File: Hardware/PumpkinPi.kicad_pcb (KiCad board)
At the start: 2 copper layers, 12.1 x 13.3 mm, 30 parts, among them J1 Conn_01x02_Male, J2 Conn_01x04, J3 Micro_SD_Card, U1 F1C100s, U2 EA3036, Y1 Crystal_GND24

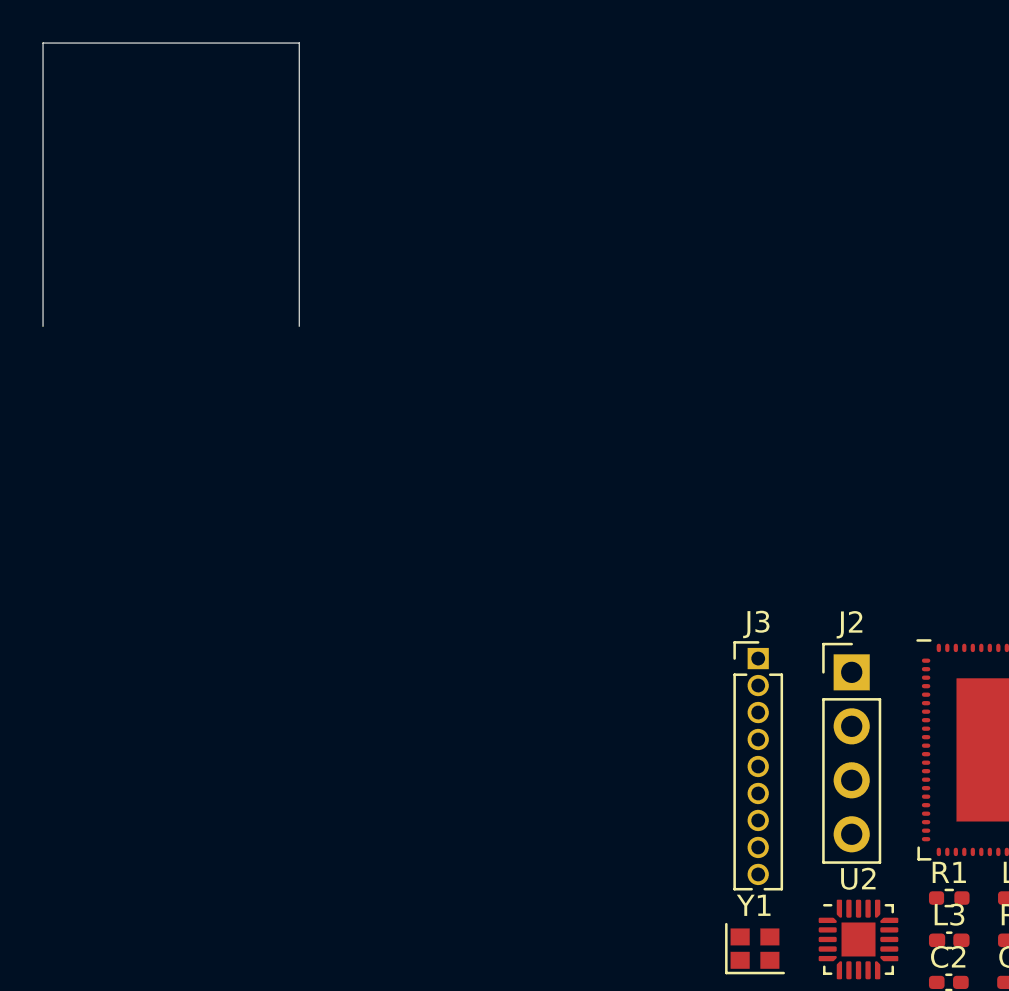
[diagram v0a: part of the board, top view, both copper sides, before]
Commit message: USB connector
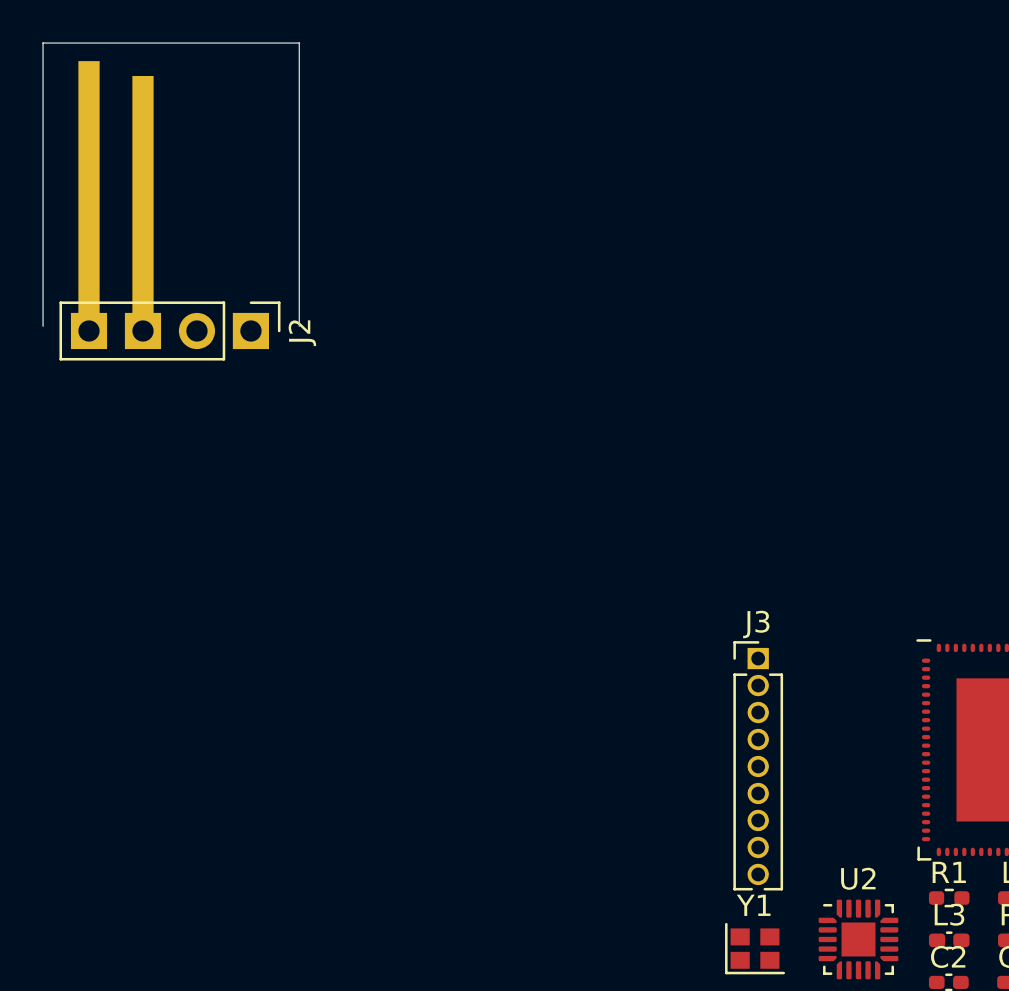
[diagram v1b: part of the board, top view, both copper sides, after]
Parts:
- moved J2 32.5 mm to (109.8, 83.6), turned to 270 degrees

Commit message: progress on wiring
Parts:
- U1: moved to B.Cu
- moved U1 42.0 mm to (106.0, 91.4)
- moved R1 35.4 mm to (176.9, 119.1)
- moved R2 33.8 mm to (185.4, 118.1)
- moved C4 31.3 mm to (181.6, 124.5)
- moved J3 29.8 mm to (104.1, 102.9)
- moved R3 28.8 mm to (181.6, 113.0)
- moved C1 21.7 mm to (174.0, 112.8)
- moved C2 20.8 mm to (155.3, 130.7)
- moved C3 20.8 mm to (158.5, 130.7)
- moved L1 20.4 mm to (168.9, 116.8)
- moved L3 17.6 mm to (146.1, 129.5)
- moved L2 15.5 mm to (145.5, 125.7)
- moved R5 14.3 mm to (157.5, 120.7)
- moved U2 11.0 mm to (133.3, 121.9)
- moved J1 6.75 mm to (149.9, 94.0)
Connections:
- C1 pad 2: GND -> /FB1
- C2 pad 2: GND -> /FB1
- C3 pad 2: GND -> /FB1
- R1 pad 2: GND -> /FB1
- R2 pad 1: GND -> /FB1
- R3 pad 2: GND -> /FB1
- R4 pad 1: GND -> /FB1
- R5 pad 2: GND -> /FB1
- R6 pad 1: GND -> /FB1
- U2 pad 14: GND -> /FB1

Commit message: wiring in progress
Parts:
- moved R8 53.9 mm to (202.4, 101.8)
- moved C12 49.8 mm to (202.2, 112.0)
- moved C7 44.6 mm to (130.1, 134.9), turned to 90 degrees
- moved C6 39.0 mm to (181.1, 133.9)
- moved R6 39.0 mm to (174.6, 137.8), turned to 270 degrees
- moved Y1 33.6 mm to (108.5, 90.1), turned to 90 degrees
- moved C11 33.4 mm to (190.3, 89.9)
- moved C5 32.8 mm to (179.3, 125.0)
- moved R4 32.8 mm to (174.5, 128.6), turned to 270 degrees
- moved C10 30.8 mm to (143.9, 134.7), turned to 90 degrees
- moved C9 30.5 mm to (138.3, 135.0), turned to 270 degrees
- moved C8 25.7 mm to (133.9, 134.9), turned to 90 degrees
- moved L3 22.1 mm to (167.8, 133.8), turned to 180 degrees
- moved R5 22.1 mm to (174.9, 134.3), turned to 270 degrees
- moved L2 21.8 mm to (167.2, 124.2)
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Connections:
- C2 pad 2: /FB1 -> /FB2
- C3 pad 2: /FB1 -> /FB3
- L2 pad 2: /LX1 -> /LX2
- L3 pad 2: /LX1 -> /LX3
- R3 pad 2: /FB1 -> /FB2
- R4 pad 1: /FB1 -> /FB2
- R5 pad 2: /FB1 -> /FB3
- R6 pad 1: /FB1 -> /FB3

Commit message: progress ...
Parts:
- removed C1, C2, C3: 220p, Capacitor_SMD:C_0402_1005Metric_Pad0.74x0.62mm_HandSolder
- removed C10: 1u, Capacitor_SMD:C_0402_1005Metric_Pad0.74x0.62mm_HandSolder
- removed C11, C12: 30p, Capacitor_SMD:C_0402_1005Metric_Pad0.74x0.62mm_HandSolder
- removed C4, C5, C6, C7, C8, C9: 10u, Capacitor_SMD:C_0402_1005Metric_Pad0.74x0.62mm_HandSolder
- removed J1: Conn_01x02_Male, Connector_PinHeader_1.27mm:PinHeader_1x02_P1.27mm_Vertical
- removed J2: Conn_01x04, Connector_PinHeader_2.54mm:PinHeader_1x04_P2.54mm_Vertical
- removed J3: Micro_SD_Card, Connector_PinHeader_1.27mm:PinHeader_1x09_P1.27mm_Vertical
- removed L1, L2, L3: 1.5u, Inductor_SMD:L_0402_1005Metric_Pad0.77x0.64mm_HandSolder
- removed R1, R2, R3, R4, R5, R6: 100k, Resistor_SMD:R_0402_1005Metric_Pad0.72x0.64mm_HandSolder
- removed R7: R, Resistor_SMD:R_0402_1005Metric_Pad0.72x0.64mm_HandSolder
- removed R8, R9: 2k2, Resistor_SMD:R_0402_1005Metric_Pad0.72x0.64mm_HandSolder
- removed U1: F1C100s, PumpkinPi:QFN-88_EP_10x10_Pitch0.4mm
- removed U2: EA3036, Package_DFN_QFN:QFN-20-1EP_3x3mm_P0.45mm_EP1.6x1.6mm
- removed Y1: Crystal_GND24, Crystal:Crystal_SMD_2016-4Pin_2.0x1.6mm
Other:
- board outline removed
- net class Default: trace_width 0.25 -> 0.2; via_dia 0.8 -> 0.4; via_drill 0.4 -> 0.3

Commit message: schemqtic finished, routing started
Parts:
- added C1: 1u, Capacitor_SMD:C_0402_1005Metric_Pad0.74x0.62mm_HandSolder, F.Cu at (159.8, 86.5)
- added C11: 30p, Capacitor_SMD:C_0402_1005Metric_Pad0.74x0.62mm_HandSolder, F.Cu at (162.2, 81.3)
- added C12: 30p, Capacitor_SMD:C_0402_1005Metric_Pad0.74x0.62mm_HandSolder, F.Cu at (162.2, 79.1)
- added C2: 1u, Capacitor_SMD:C_0402_1005Metric_Pad0.74x0.62mm_HandSolder, F.Cu at (159.8, 82.0)
- added C3: 1u, Capacitor_SMD:C_0402_1005Metric_Pad0.74x0.62mm_HandSolder, F.Cu at (159.8, 88.7)
- added J1: Conn_01x02_Male, Connector_PinHeader_1.00mm:PinHeader_1x02_P1.00mm_Vertical, F.Cu at (162.2, 90.9)
- added J2: Conn_01x04, Connector_PinHeader_2.54mm:PinHeader_1x04_P2.54mm_Vertical, F.Cu at (159.9, 92.0)
- added J3: 0475710001, MOLEX_0475710001, F.Cu at (153.0, 84.2)
- added R7: 51k, Resistor_SMD:R_0402_1005Metric_Pad0.72x0.64mm_HandSolder, F.Cu at (162.2, 88.1)
- added R8: 2k2, Resistor_SMD:R_0402_1005Metric_Pad0.72x0.64mm_HandSolder, F.Cu at (162.2, 83.6)
- added R9: 2k2, Resistor_SMD:R_0402_1005Metric_Pad0.72x0.64mm_HandSolder, F.Cu at (162.2, 85.8)
- added U1: F1C100s, PumpkinPi:QFN-88_EP_10x10_Pitch0.4mm, B.Cu at (155.7, 84.0)
- added U2: TPS717xx, Package_TO_SOT_SMD:SOT-353_SC-70-5, F.Cu at (157.7, 86.1)
- added U3: TPS717xx, Package_TO_SOT_SMD:SOT-353_SC-70-5, F.Cu at (157.7, 83.3)
- added U4: TPS717xx, Package_TO_SOT_SMD:SOT-353_SC-70-5, F.Cu at (157.7, 89.0)
- added Y1: Crystal_GND24, Crystal:Crystal_SMD_5032-4Pin_5.0x3.2mm, F.Cu at (158.9, 79.9)
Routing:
- net GND: track 0.00 -> 63.4 mm
- net /SVREF: track 0.00 -> 18.0 mm, vias 0 -> 2
- net /USB_VBUS: track 0.00 -> 15.9 mm
- net +1V1: track 0.00 -> 13.3 mm, vias 0 -> 2
- net +3V3: track 0.00 -> 12.3 mm, vias 0 -> 3
- net /SD0_D0: track 0.00 -> 11.6 mm, vias 0 -> 2
- net /SD0_D1: track 0.00 -> 11.4 mm, vias 0 -> 2
- net /SD0_D3: track 0.00 -> 11.0 mm, vias 0 -> 2
- net /SD0_CMD: track 0.00 -> 10.6 mm, vias 0 -> 2
- net /SD0_D2: track 0.00 -> 10.2 mm, vias 0 -> 2
- net /SD0_CLK: track 0.00 -> 9.45 mm, vias 0 -> 2
- net /CLKP: track 0.00 -> 8.38 mm, vias 0 -> 2
- net +2V5: track 0.00 -> 8.19 mm
- net /CLKN: track 0.00 -> 5.99 mm, vias 0 -> 2
- net /USB_DP: track 0.00 -> 5.80 mm
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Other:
- copper layers 2 -> 4
- net class Default: via_drill 0.3 -> 0.2
- rule via_min_drill: 0.3 -> 0.2

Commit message: minor changes
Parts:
- added J4: Conn_01x05, Connector_PinHeader_2.54mm:PinHeader_1x05_P2.54mm_Vertical, F.Cu at (114.0, 98.7)
- added J5: Conn_01x05, Connector_PinHeader_2.54mm:PinHeader_1x05_P2.54mm_Vertical, F.Cu at (100.7, 87.0)
- added J6: Conn_01x05, Connector_PinHeader_2.54mm:PinHeader_1x05_P2.54mm_Vertical, F.Cu at (98.3, 98.7)
- J1: footprint Connector_PinHeader_1.00mm:PinHeader_1x02_P1.00mm_Vertical -> Jumper:SolderJumper-2_P1.3mm_Open_Pad1.0x1.5mm
- J2: footprint Connector_PinHeader_2.54mm:PinHeader_1x04_P2.54mm_Vertical -> PumpkinPi:USB_PCB
- moved C1 70.8 mm to (90.3, 99.8), turned to 0 degrees
- moved C3 69.7 mm to (90.4, 95.9), turned to 0 degrees
- moved C2 69.7 mm to (90.8, 91.8)
- moved U4 66.7 mm to (91.1, 85.0), turned to 90 degrees
- moved J2 58.3 mm to (102.4, 101.5), turned to 90 degrees
- moved U3 56.9 mm to (101.6, 92.8), turned to 90 degrees
- moved C12 55.3 mm to (108.6, 92.7), turned to 180 degrees
- moved U2 53.7 mm to (104.4, 92.8), turned to 90 degrees
- moved C11 52.0 mm to (111.5, 92.7), turned to 0 degrees
- moved U1 50.5 mm to (106.2, 94.2)
- moved Y1 50.1 mm to (109.9, 90.3), turned to 180 degrees
- moved J3 48.5 mm to (106.3, 97.5), turned to 180 degrees
- moved J1 45.4 mm to (116.7, 90.8), turned to 90 degrees
- moved R9 44.2 mm to (158.2, 129.8), turned to 0 degrees
- moved R7 42.3 mm to (155.0, 129.8), turned to 0 degrees
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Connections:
- J2 pad 2: /USB_DM -> /USB_P
- J2 pad 3: /USB_DP -> /USB_N
- U1 pad 13: (no net) -> /PD7
- U1 pad 14: (no net) -> /PD8
- U1 pad 15: (no net) -> /PD9
- U1 pad 16: (no net) -> /PD10
- U1 pad 37: (no net) -> /SDA
- U1 pad 38: (no net) -> /SCL
- U1 pad 48: (no net) -> /TX
- U1 pad 49: (no net) -> /RX
- U1 pad 59: (no net) -> /SPI_CLK
- U1 pad 60: (no net) -> /SPI_CS
- U1 pad 61: (no net) -> /SPI_MISO
- U1 pad 62: (no net) -> /SPI_MOSI
- U1 pad 68: /USB_DM -> /USB_N
- U1 pad 69: /USB_DP -> /USB_P
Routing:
- net GND: track 63.4 -> 34.0 mm
- net /SVREF: track 18.0 -> 0.54 mm, vias 2 -> 1
- net /USB_VBUS: track 15.9 -> 0.00 mm
- net /CLKP: track 8.38 -> 0.00 mm, vias 2 -> 0
- net /SD0_D1: track 11.4 -> 4.16 mm, vias 2 -> 1
- net /SD0_D0: track 11.6 -> 5.22 mm, vias 2 -> 1
- net /CLKN: track 5.99 -> 0.00 mm, vias 2 -> 0
- net /USB_P: track 0.00 -> 5.98 mm
- net +1V1: track 13.3 -> 7.33 mm, vias 2 -> 1
- net +3V3: track 12.3 -> 18.2 mm
- net /USB_DP: track 5.80 -> 0.00 mm
- net /USB_DM: track 4.03 -> 0.00 mm
- net /USB_N: track 0.00 -> 3.98 mm
- net /SD0_CLK: track 9.45 -> 6.61 mm, vias 2 -> 1
- net +2V5: track 8.19 -> 5.98 mm, vias 0 -> 1
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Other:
- board outline added: 12.4 x 14.8 mm

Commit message: placemnt done
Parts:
- removed J1: Conn_01x02_Male, Jumper:SolderJumper-2_P1.3mm_Open_Pad1.0x1.5mm
- moved R9 65.5 mm to (106.6, 89.6), turned to 270 degrees
- moved R8 63.2 mm to (104.6, 88.9)
- moved R7 59.4 mm to (107.8, 93.7)
- moved C1 16.9 mm to (104.6, 90.8)
- moved C3 15.9 mm to (106.1, 93.4), turned to 90 degrees
- moved U4 15.5 mm to (104.4, 92.8)
- moved C2 13.9 mm to (104.6, 89.8)
- moved U3 3.02 mm to (101.9, 89.8), turned to 0 degrees
- moved U2 2.88 mm to (101.5, 92.8)
- moved C11 0.90 mm to (112.2, 93.3), turned to 270 degrees
- moved Y1 0.24 mm to (109.8, 90.1)
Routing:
- net /RESET: track 1.00 -> 16.0 mm, vias 1 -> 2
- net GND: track 34.0 -> 48.7 mm
- net /CLKP: track 0.00 -> 5.59 mm
- net /CLKN: track 0.00 -> 4.18 mm, vias 0 -> 1
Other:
- board size 12.4 x 14.8 mm -> 19.4 x 29.7 mm

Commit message: routing done
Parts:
- moved J5 0.46 mm to (101.1, 86.7)
- moved U3 0.24 mm to (101.7, 89.7)
- moved U2 0.14 mm to (101.5, 92.7)
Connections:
- J5 pad 3: /RX -> /TX
- J5 pad 4: /TX -> /RX
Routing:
- net GND: track 48.7 -> 82.4 mm, vias 0 -> 1
- net +3V3: track 18.2 -> 43.8 mm, vias 3 -> 5
- net /USB_VBUS: track 0.00 -> 24.6 mm, vias 0 -> 1
- net +1V1: track 7.33 -> 24.9 mm, vias 1 -> 3
- net +2V5: track 5.98 -> 22.1 mm, vias 1 -> 2
- net /TX: track 0.00 -> 8.39 mm
- net /SDA: track 0.00 -> 7.92 mm
- net /PD7: track 0.00 -> 7.35 mm
- net /RX: track 0.00 -> 7.01 mm
- net /SPI_CLK: track 0.00 -> 6.06 mm
- net /SCL: track 0.00 -> 5.88 mm
- net /PD8: track 0.00 -> 4.64 mm
- net /SPI_CS: track 0.00 -> 4.05 mm
- net /SPI_MOSI: track 0.00 -> 3.81 mm
- net /PD10: track 0.00 -> 3.67 mm
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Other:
- board size 19.4 x 29.7 mm -> 18.4 x 29.3 mm
